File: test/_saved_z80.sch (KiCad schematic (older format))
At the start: 48 parts, among them U1 74AHC1G14

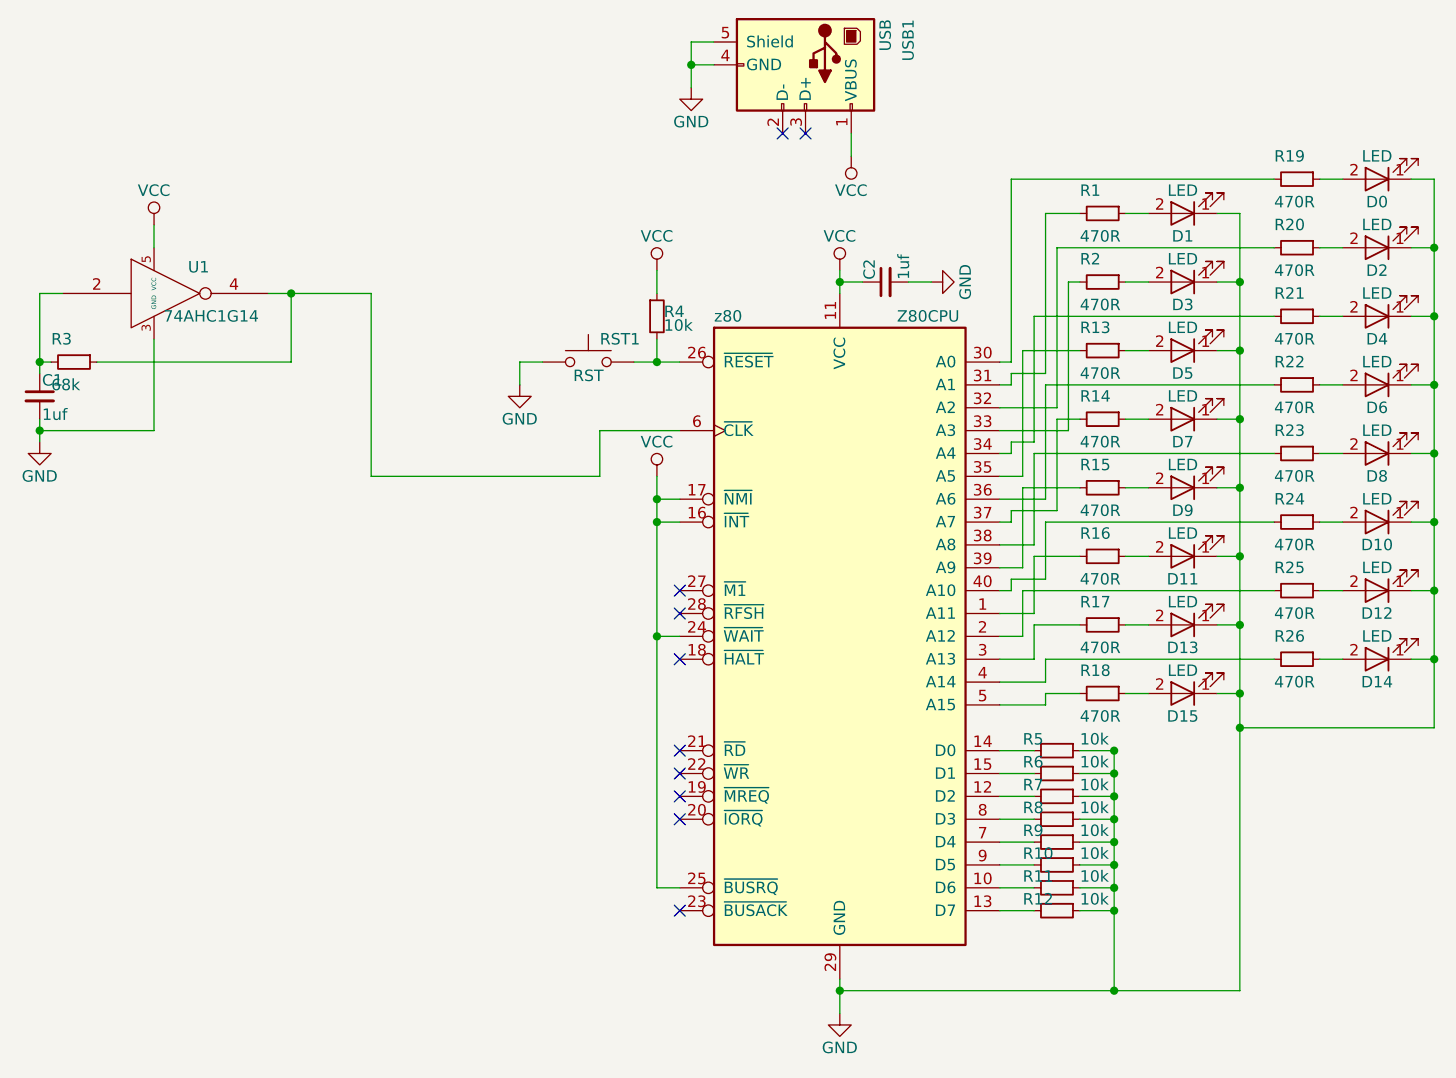
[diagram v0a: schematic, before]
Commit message: Renumber data pulldowns and address LEDs to match bits
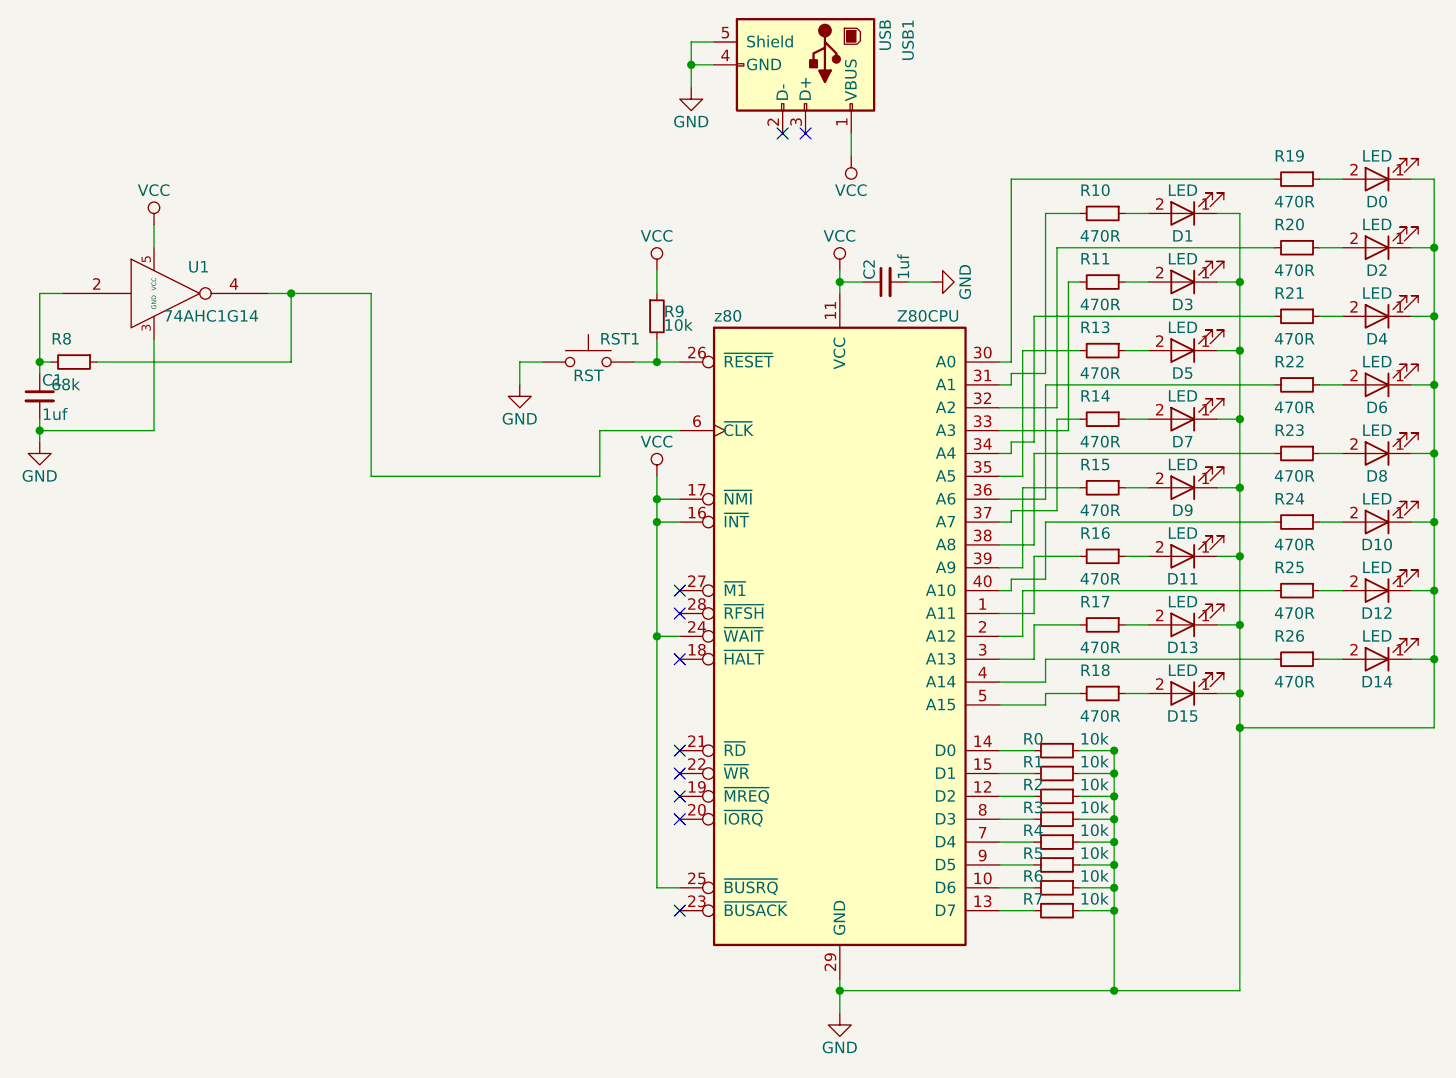
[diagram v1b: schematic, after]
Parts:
- renumbered R5 to R0, R6 to R1, R1 to R10, R2 to R11, R7 to R2, R8 to R3, R9 to R4, R10 to R5, R11 to R6, R12 to R7, R3 to R8, R4 to R9
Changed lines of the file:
@@
 $EndComp
 $Comp
-L R_Small R5
+L R_Small R0
 U 1 1 59450825
 P 6300 4750
-F 0 "R5" V 6250 4600 50  0000 L CNN
+F 0 "R0" V 6250 4600 50  0000 L CNN
 F 1 "10k" V 6250 4850 50  0000 L CNN
 F 2 "Resistors_SMD:R_0805_HandSoldering" H 6300 4750 50  0001 C CNN
@@
 $EndComp
 $Comp
-L R_Small R6
+L R_Small R1
 U 1 1 5945082B
 P 6300 4850
-F 0 "R6" V 6250 4700 50  0000 L CNN
+F 0 "R1" V 6250 4700 50  0000 L CNN
 F 1 "10k" V 6250 4950 50  0000 L CNN
 F 2 "Resistors_SMD:R_0805_HandSoldering" H 6300 4850 50  0001 C CNN
@@
 $EndComp
 $Comp
-L R_Small R7
+L R_Small R2
 U 1 1 59450831
 P 6300 4950
-F 0 "R7" V 6250 4800 50  0000 L CNN
+F 0 "R2" V 6250 4800 50  0000 L CNN
 F 1 "10k" V 6250 5050 50  0000 L CNN
 F 2 "Resistors_SMD:R_0805_HandSoldering" H 6300 4950 50  0001 C CNN
@@
 $EndComp
 $Comp
-L R_Small R8
+L R_Small R3
 U 1 1 59450837
 P 6300 5050
-F 0 "R8" V 6250 4900 50  0000 L CNN
+F 0 "R3" V 6250 4900 50  0000 L CNN
 F 1 "10k" V 6250 5150 50  0000 L CNN
 F 2 "Resistors_SMD:R_0805_HandSoldering" H 6300 5050 50  0001 C CNN
@@
 $EndComp
 $Comp
-L R_Small R9
+L R_Small R4
 U 1 1 5945083D
 P 6300 5150
-F 0 "R9" V 6250 5000 50  0000 L CNN
+F 0 "R4" V 6250 5000 50  0000 L CNN
 F 1 "10k" V 6250 5250 50  0000 L CNN
 F 2 "Resistors_SMD:R_0805_HandSoldering" H 6300 5150 50  0001 C CNN
@@
 $EndComp
 $Comp
-L R_Small R10
+L R_Small R5
 U 1 1 59450843
 P 6300 5250
-F 0 "R10" V 6250 5100 50  0000 L CNN
+F 0 "R5" V 6250 5100 50  0000 L CNN
 F 1 "10k" V 6250 5350 50  0000 L CNN
 F 2 "Resistors_SMD:R_0805_HandSoldering" H 6300 5250 50  0001 C CNN
@@
 $EndComp
 $Comp
-L R_Small R11
+L R_Small R6
 U 1 1 59450849
 P 6300 5350
-F 0 "R11" V 6250 5200 50  0000 L CNN
+F 0 "R6" V 6250 5200 50  0000 L CNN
 F 1 "10k" V 6250 5450 50  0000 L CNN
 F 2 "Resistors_SMD:R_0805_HandSoldering" H 6300 5350 50  0001 C CNN
@@
 $EndComp
 $Comp
-L R_Small R12
+L R_Small R7
 U 1 1 5945084F
 P 6300 5450
-F 0 "R12" V 6250 5300 50  0000 L CNN
+F 0 "R7" V 6250 5300 50  0000 L CNN
 F 1 "10k" V 6250 5550 50  0000 L CNN
 F 2 "Resistors_SMD:R_0805_HandSoldering" H 6300 5450 50  0001 C CNN
@@
 NoConn ~ 4650 4150
 $Comp
-L R_Small R4
+L R_Small R9
 U 1 1 59458696
 P 4550 2850
-F 0 "R4" H 4580 2870 50  0000 L CNN
+F 0 "R9" H 4580 2870 50  0000 L CNN
 F 1 "10k" H 4580 2810 50  0000 L CNN
 F 2 "Resistors_SMD:R_0805_HandSoldering" H 4550 2850 50  0001 C CNN
@@
 $EndComp
 $Comp
-L R_Small R3
+L R_Small R8
 U 1 1 59459C0E
 P 2000 3050
-F 0 "R3" V 1900 2950 50  0000 L CNN
+F 0 "R8" V 1900 2950 50  0000 L CNN
 F 1 "68k" V 2100 2950 50  0000 L CNN
 F 2 "Resistors_SMD:R_0805_HandSoldering" H 2000 3050 50  0001 C CNN
@@
 	6700 3900 6600 3900
 $Comp
-L R_Small R1
+L R_Small R10
 U 1 1 5954462D
 P 6500 2400
-F 0 "R1" V 6400 2300 50  0000 L CNN
+F 0 "R10" V 6400 2300 50  0000 L CNN
 F 1 "470R" V 6600 2300 50  0000 L CNN
 F 2 "Resistors_SMD:R_0805_HandSoldering" H 6500 2400 50  0001 C CNN
@@
 $EndComp
 $Comp
-L R_Small R2
+L R_Small R11
 U 1 1 59544633
 P 6500 2700
-F 0 "R2" V 6400 2600 50  0000 L CNN
+F 0 "R11" V 6400 2600 50  0000 L CNN
 F 1 "470R" V 6600 2600 50  0000 L CNN
 F 2 "Resistors_SMD:R_0805_HandSoldering" H 6500 2700 50  0001 C CNN
